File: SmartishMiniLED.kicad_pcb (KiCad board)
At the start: 2 copper layers, 30 x 60 mm, 35 parts, among them J1 USB_C_Receptacle_USB2.0, J2 BUTTON, J3 Screw_Terminal_01x03, J4 Conn_01x02, P1 NeopixelStripPads, P2 NeopixelStripPads, Q1 MMBT2222, Q2 MMBT2222, Q3 IRLML6344, Q4 IRF7410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

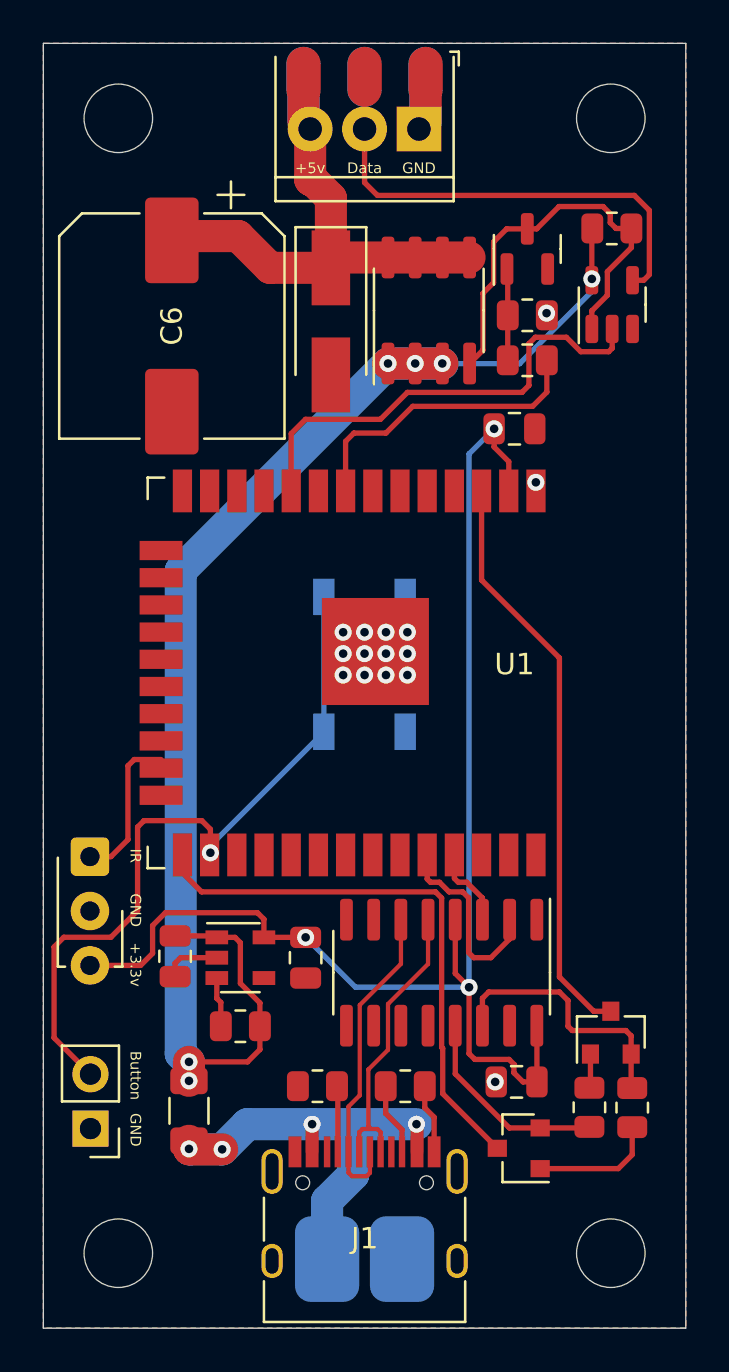
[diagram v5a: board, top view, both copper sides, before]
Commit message: Stopped putting vias directly on pads, can cause productions errors
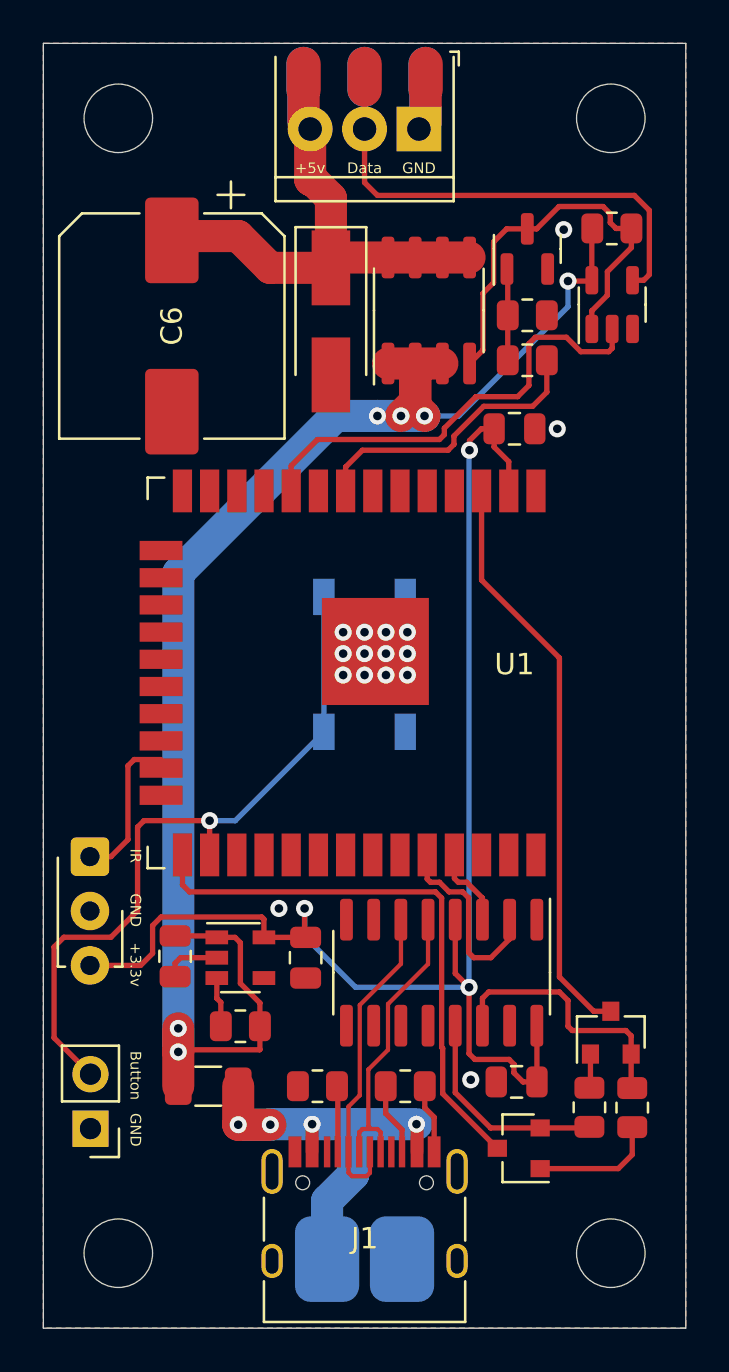
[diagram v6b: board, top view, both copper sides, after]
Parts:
- moved F1 1.46 mm to (143.7, 104.7), turned to 180 degrees
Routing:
- net +5V: track 66.2 -> 73.2 mm
- net +3V3: track 63.9 -> 66.7 mm
- net /+5V_In: track 22.5 -> 21.0 mm
- net /NEOPIXEL: track 21.5 -> 20.8 mm
- net /DTR: track 9.51 -> 10.0 mm
- net GND: vias 15 -> 16

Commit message: Updated teh version number
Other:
- board text added: "${version_name}"
- board text removed: "v1.0"
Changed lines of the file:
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@@
   (property "date" "2022-08-03")
   (property "version" "bd43bc3")
+  (property "version_name" "v1.1")
   (net 0 "")
   (net 1 "VBUS")
@@
   )
   (gr_rect (start 166 116) (end 136 56) (layer "Edge.Cuts") (width 0.05) (fill none))
-  (gr_text "v1.0" (at 149.606 68.3904) (layer "B.SilkS")
+  (gr_text "${version_name}" (at 151.2 68.4) (layer "B.SilkS")
     (effects (font (size 1 1) (thickness 0.2)) (justify mirror))
   )
@@
     (effects (font (size 0.6 0.6) (thickness 0.125)) (justify mirror))
   )
-  (gr_text "Smartish MiniLED" (at 149.352 66.1044) (layer "B.SilkS")
+  (gr_text "Smartish MiniLED" (at 151 66) (layer "B.SilkS")
     (effects (font (size 1.5 1.5) (thickness 0.3) italic) (justify mirror))
   )
